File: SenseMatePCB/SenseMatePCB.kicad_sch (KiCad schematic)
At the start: 1 part

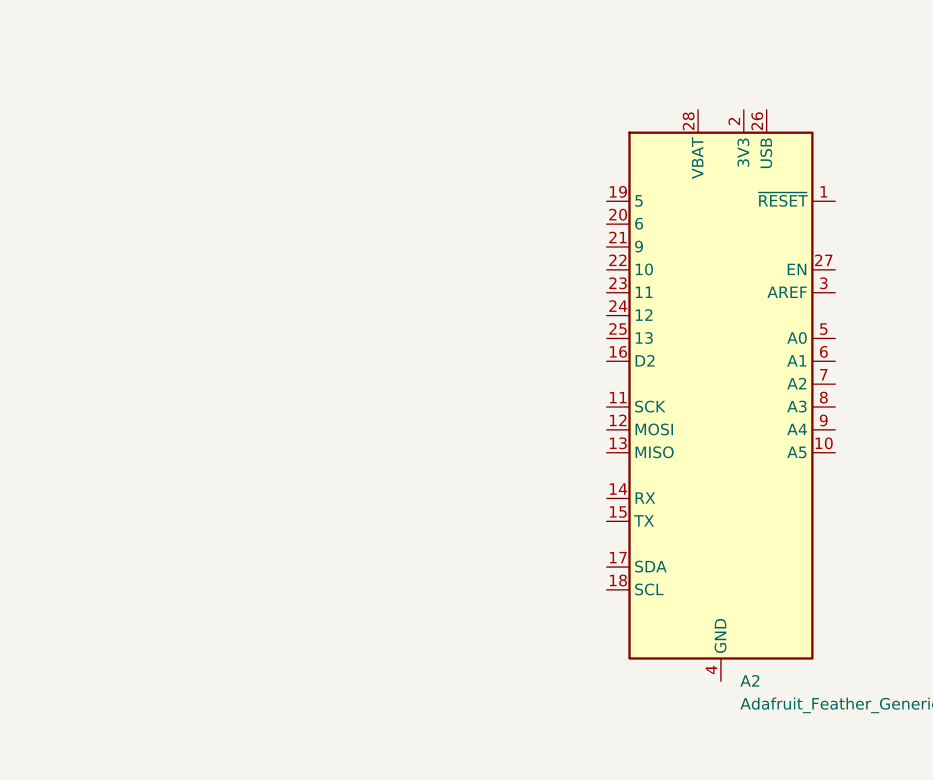
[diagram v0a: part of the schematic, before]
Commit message: Added sound buzzer to schmatic
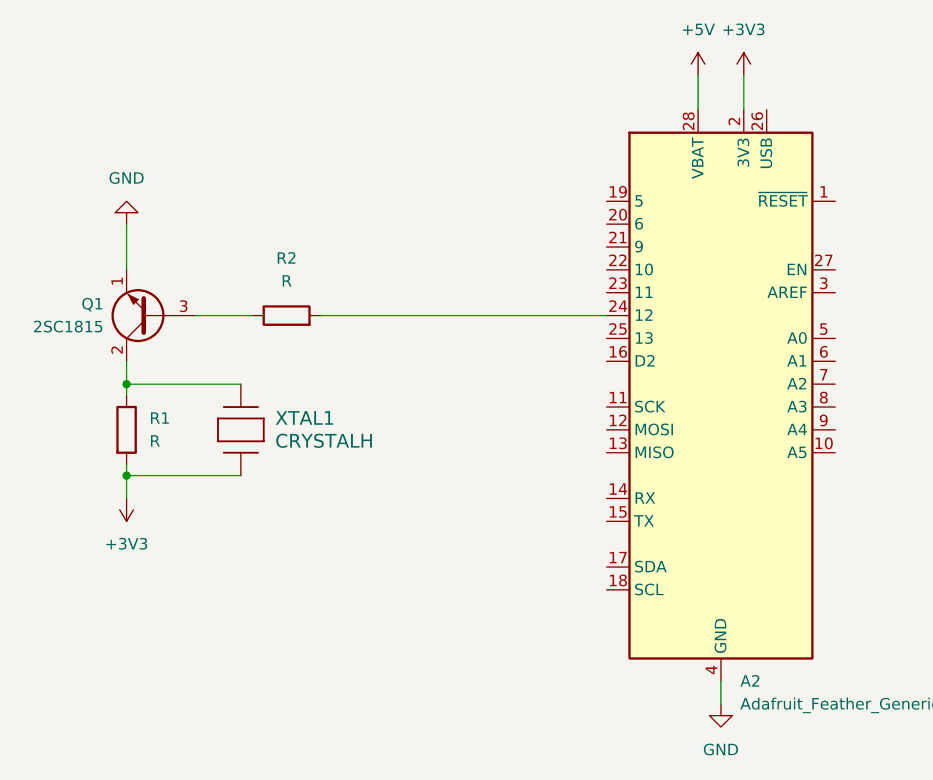
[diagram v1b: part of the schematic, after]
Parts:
- added Q1: 2SC1815, Package_TO_SOT_THT:TO-92_Inline, symbol Transistor_BJT:2SC1815
- added R1, R2: R, symbol Device:R
- added XTAL1: CRYSTALH, XTAL_PS1240P02BT_TDK, symbol FeatherSense_Sound_Buzzer:CRYSTALH
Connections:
- net +3V3: now reaches A2.2 (3V3)
- net +3V3: now also R1.2, XTAL1.1
- net at A2.24 (12): now also R2.2
- net +5V: now reaches A2.28 (VBAT)
- net GND: now reaches A2.4 (GND)
- net GND: now also Q1.1 (E)
- new net: Q1.2 (C), R1.1, XTAL1.2
- new net: Q1.3 (B), R2.1

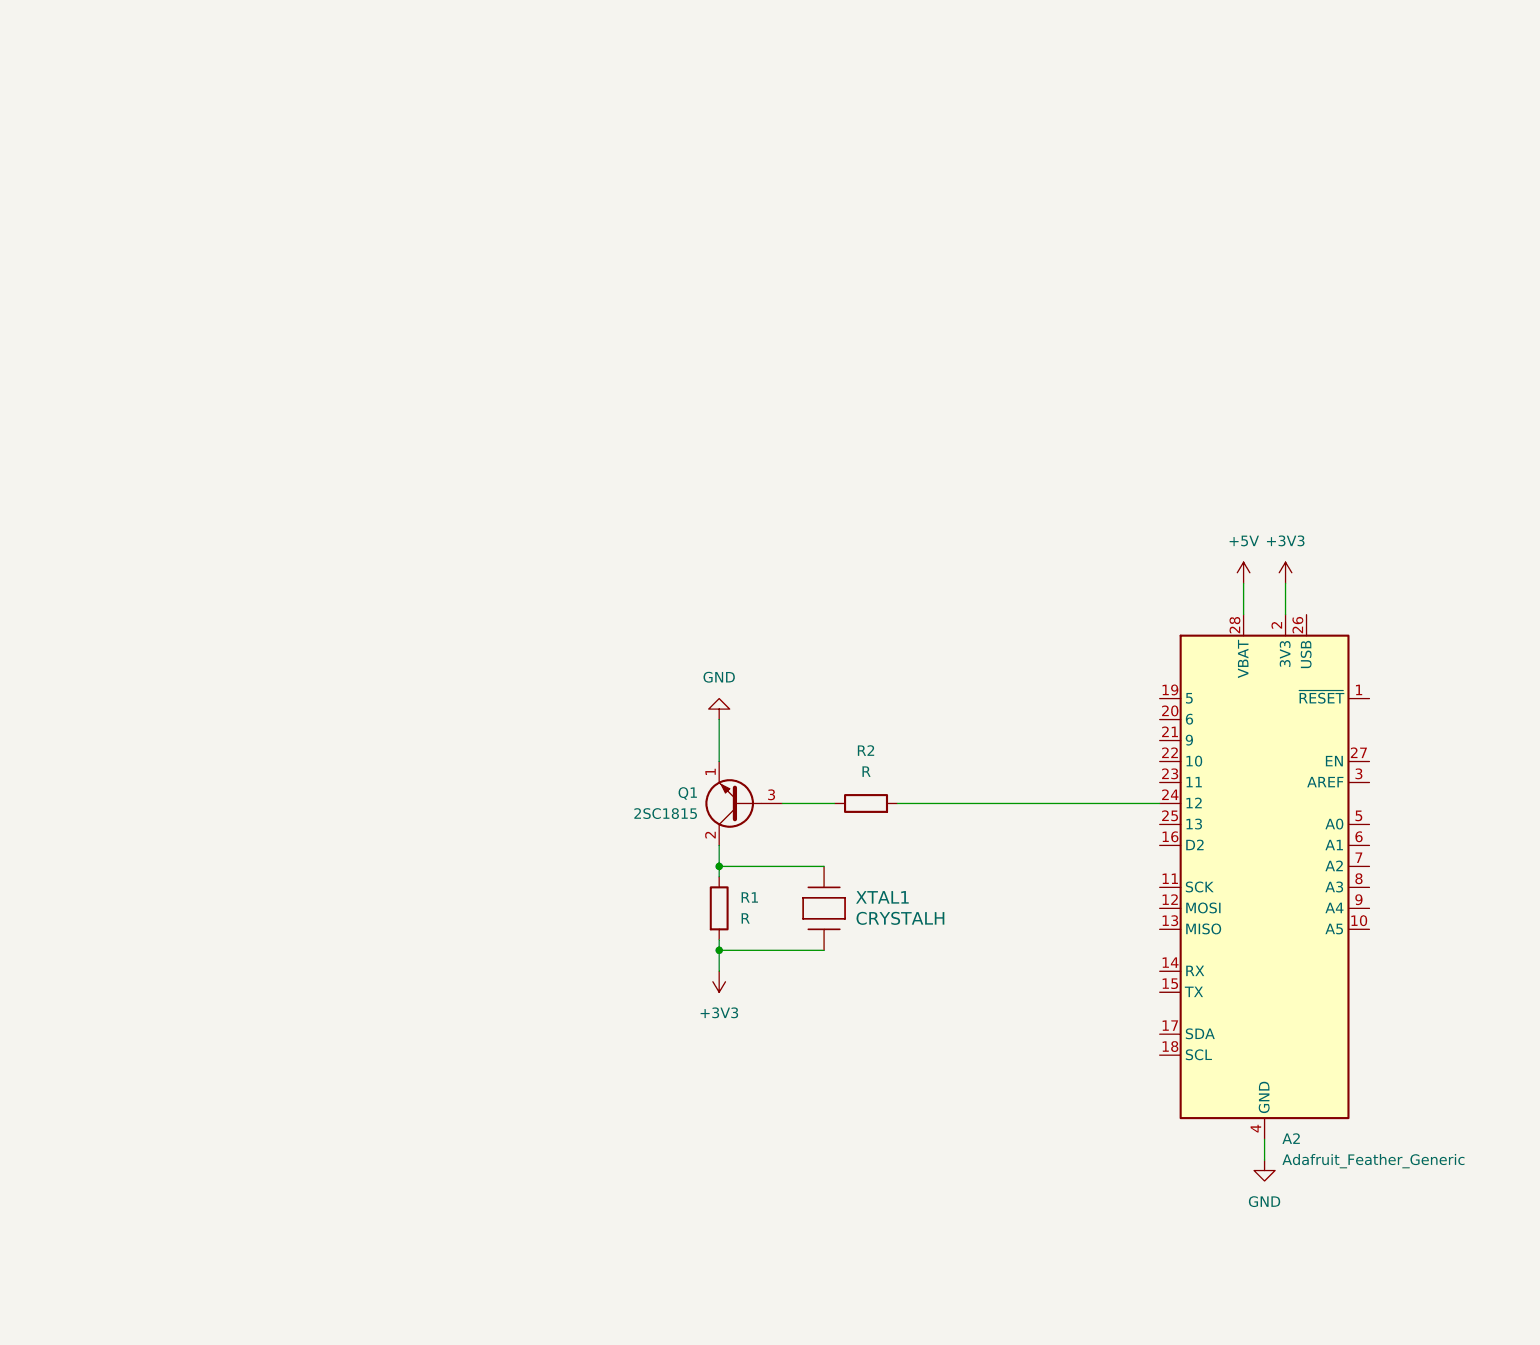
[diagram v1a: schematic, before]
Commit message: schematic nearly finished, only lcd needs to be added
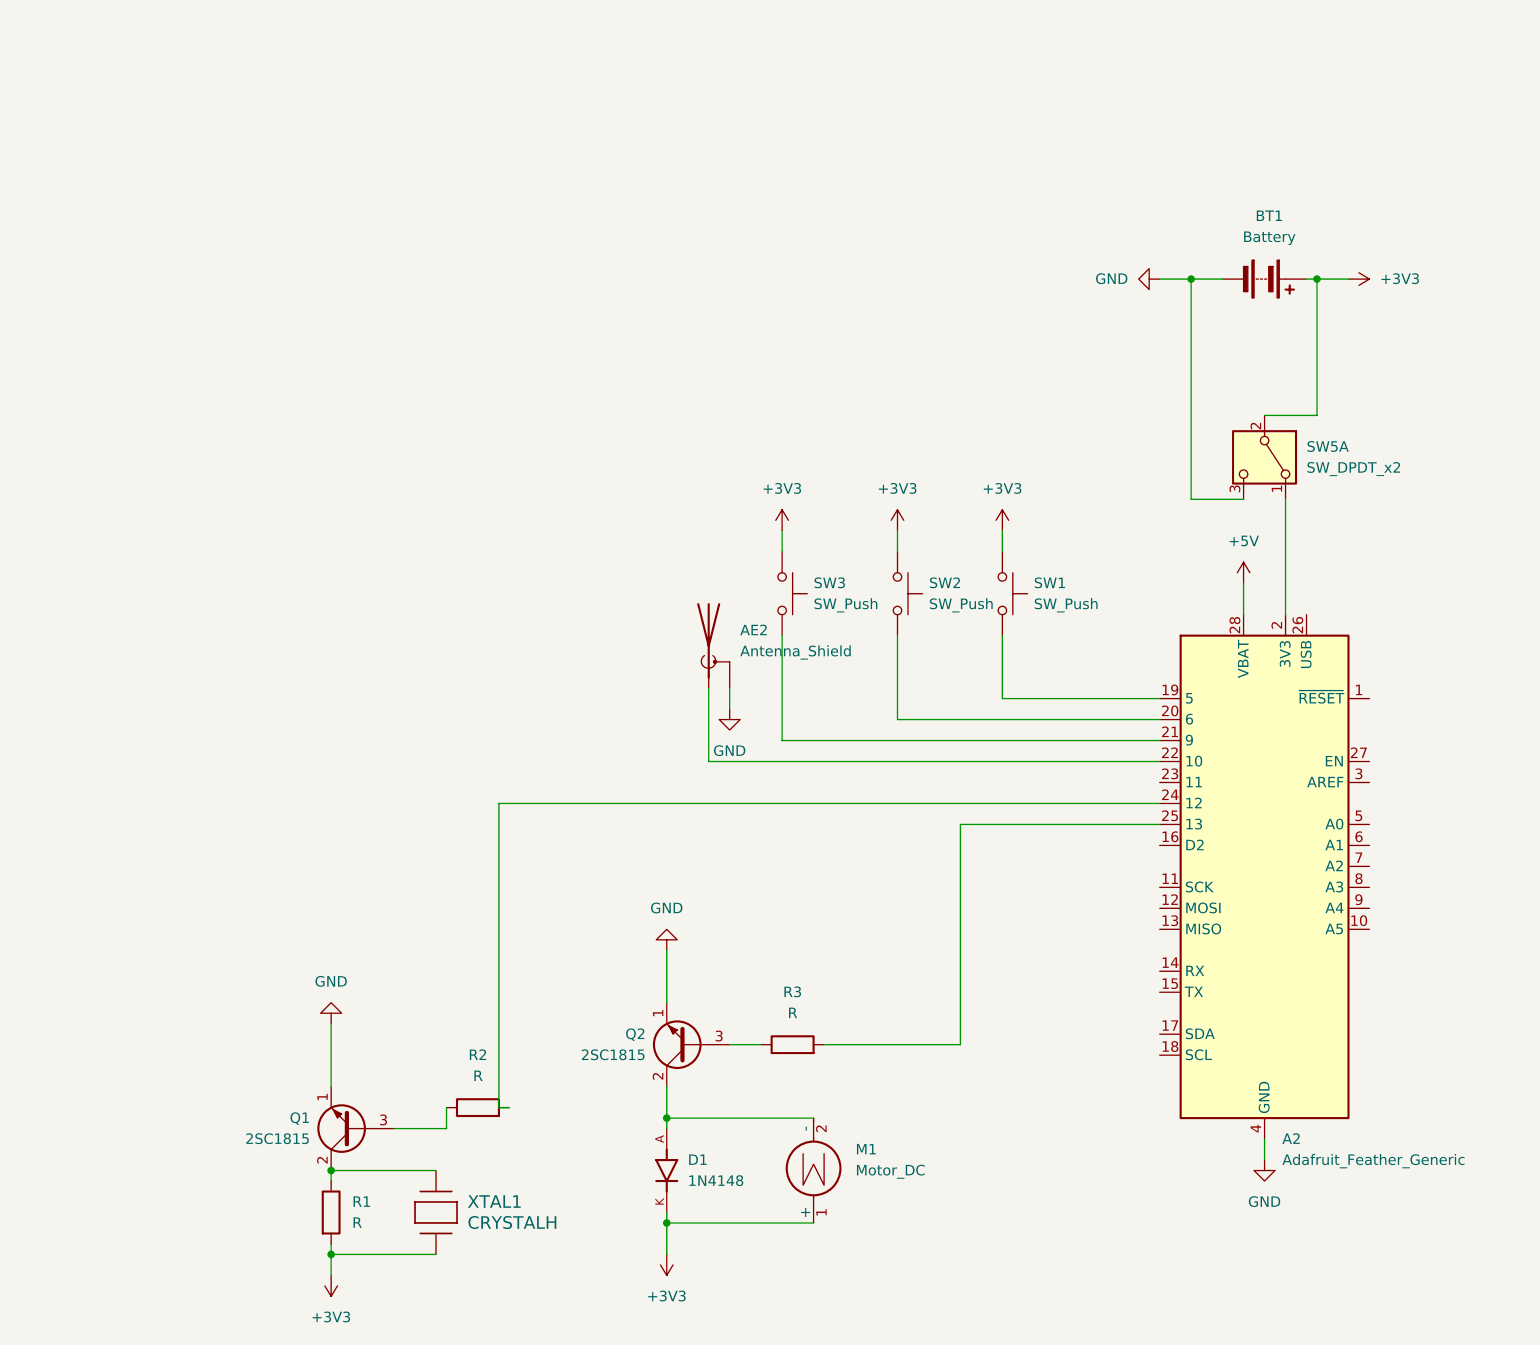
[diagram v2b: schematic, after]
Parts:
- added AE2: Antenna_Shield, symbol Device:Antenna_Shield
- added BT1: Battery, symbol Device:Battery
- added D1: 1N4148, 1N4148:DIOAD753W49L380D172B, symbol FeatherSense_1N4148:1N4148
- added M1: Motor_DC, symbol Motor:Motor_DC
- added Q2: 2SC1815, Package_TO_SOT_THT:TO-92_Inline, symbol Transistor_BJT:2SC1815
- added R3: R, symbol Device:R
- added SW1, SW2, SW3: SW_Push, symbol Switch:SW_Push
- added SW5: SW_DPDT_x2, symbol Switch:SW_DPDT_x2
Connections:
- net +3V3: now also BT1.1 (+), D1.K, M1.1 (+), SW1.1, SW2.1, SW3.1, SW5.2 (B); no longer A2.2 (3V3)
- net GND: now also AE2.2 (Shield), BT1.2 (-), Q2.1 (E), SW5.3 (C)
- net at A2.19 (5): now also SW1.2
- net at A2.20 (6): now also SW2.2
- net at A2.21 (9): now also SW3.2
- net at A2.22 (10): now also AE2.1 (A)
- net at A2.25 (13): now also R3.2
- new net: A2.2 (3V3), SW5.1 (A)
- new net: D1.A, M1.2 (-), Q2.2 (C)
- new net: Q2.3 (B), R3.1
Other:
- moved on the sheet: Q1, R1, R2, XTAL1

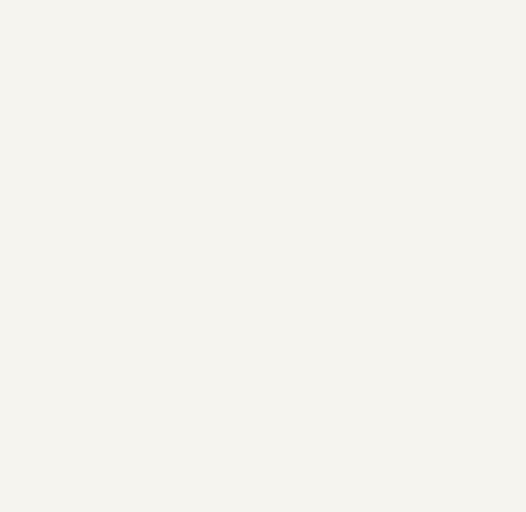
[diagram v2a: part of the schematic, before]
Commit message: added own version of butto
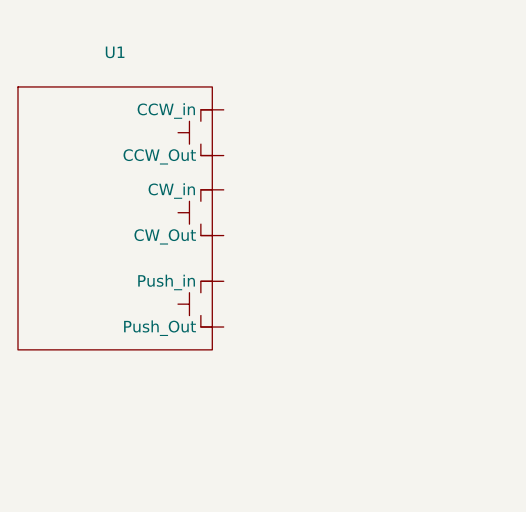
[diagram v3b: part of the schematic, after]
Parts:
- added U1: ~, symbol FeatherSense_PushButton:_1
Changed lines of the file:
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@@
+	)
+	(symbol
+		(lib_id "FeatherSense_PushButton:_1")
+		(at 59.69 60.96 0)
+		(unit 1)
+		(exclude_from_sim no)
+		(in_bom yes)
+		(on_board yes)
+		(dnp no)
+		(fields_autoplaced yes)
+		(property "Reference" "U1"
+			(at 61.595 43.18 0)
+			(effects
+				(font
+					(size 1.27 1.27)
+				)
+			)
+		)
+		(property "Value" "~"
+			(at 61.595 45.72 0)
+			(effects
+				(font
+					(size 1.27 1.27)
+				)
+			)
+		)
+		(property "Footprint" ""
+			(at 59.69 60.96 0)
+			(effects
+				(font
+					(size 1.27 1.27)
+				)
+				(hide yes)
+			)
+		)
+		(property "Datasheet" ""
+			(at 59.69 60.96 0)
+			(effects
+				(font
+					(size 1.27 1.27)
+				)
+				(hide yes)
+			)
+		)
+		(property "Description" ""
+			(at 59.69 60.96 0)
+			(effects
+				(font
+					(size 1.27 1.27)
+				)
+				(hide yes)
+			)
+		)
+		(pin ""
+		)
+		(pin ""
+		)
+		(pin ""
+		)
+		(pin ""
+		)
+		(pin ""
+		)
+		(pin ""
+		)
+		(instances
+			(project ""
+				(path "/70e40189-008f-4f72-8f4c-fe289f3548a4"
+					(reference "U1")
+					(unit 1)
+				)
+			)
+		)
 	)
 	(symbol
